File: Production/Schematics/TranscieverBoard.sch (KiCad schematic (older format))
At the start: 6 parts, among them J1 1909763-1, J2 Conn_01x10_Male, J3 Conn_01x10_Male, J4 Conn_01x10_Male, J5 Conn_01x10_Male, U1 MAX7037EGL+

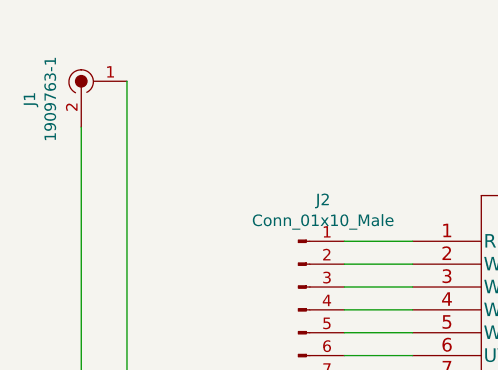
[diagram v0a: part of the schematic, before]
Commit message: Updated PCB
Updated PCB from MCX to SMA
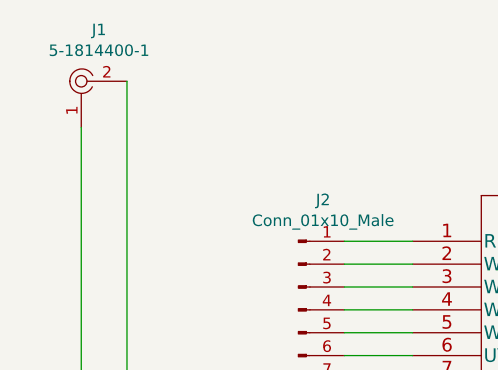
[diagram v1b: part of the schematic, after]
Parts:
- removed J1: 1909763-1, digikey-footprints:UMCoax_Pin_1909763-1, symbol dk_Coaxial-Connectors-RF:1909763-1
- added J1: 5-1814400-1, digikey-footprints:RF_SMA_RightAngle_5-1814400-1, symbol dk_Coaxial-Connectors-RF:5-1814400-1
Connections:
- net at J3.5 (Pin_5), U1.15 (RF_N): now also J1.2
- net at J3.6 (Pin_6), U1.16 (RF_P): now also J1.1
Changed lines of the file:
@@
 	2850 4150 2850 2150
-$Comp
-L dk_Coaxial-Connectors-RF:1909763-1 J1
-U 1 1 61EF2637
-P 2850 1950
-F 0 "J1" H 2928 2175 50  0000 C CNN
-F 1 "1909763-1" H 2928 2084 50  0000 C CNN
-F 2 "digikey-footprints:UMCoax_Pin_1909763-1" H 3050 2150 60  0001 L CNN
-F 3 "https://www.te.com/commerce/DocumentDelivery/DDEController?Action=srchrtrv&DocNm=1909763&DocType=Customer+Drawing&DocLang=English" H 3050 2250 60  0001 L CNN
-F 4 "A118077CT-ND" H 3050 2350 60  0001 L CNN "Digi-Key_PN"
-F 5 "1909763-1" H 3050 2450 60  0001 L CNN "MPN"
-F 6 "Connectors, Interconnects" H 3050 2550 60  0001 L CNN "Category"
-F 7 "Coaxial Connectors (RF)" H 3050 2650 60  0001 L CNN "Family"
-F 8 "https://www.te.com/commerce/DocumentDelivery/DDEController?Action=srchrtrv&DocNm=1909763&DocType=Customer+Drawing&DocLang=English" H 3050 2750 60  0001 L CNN "DK_Datasheet_Link"
-F 9 "/product-detail/en/te-connectivity-amp-connectors/1909763-1/A118077CT-ND/4729711" H 3050 2850 60  0001 L CNN "DK_Detail_Page"
-F 10 "CONN UMCC JACK STR 50OHM SMD" H 3050 2950 60  0001 L CNN "Description"
-F 11 "TE Connectivity AMP Connectors" H 3050 3050 60  0001 L CNN "Manufacturer"
-F 12 "Active" H 3050 3150 60  0001 L CNN "Status"
-	1    2850 1950
-	0    -1   1    0
-$EndComp
 $Comp
 L Connector:Conn_01x10_Male J3
@@
 Wire Wire Line
 	3050 4050 4000 4050
+$Comp
+L dk_Coaxial-Connectors-RF:5-1814400-1 J1
+U 1 1 620A4B48
+P 2850 1950
+F 0 "J1" H 2928 2175 50  0000 C CNN
+F 1 "5-1814400-1" H 2928 2084 50  0000 C CNN
+F 2 "digikey-footprints:RF_SMA_RightAngle_5-1814400-1" H 3050 2150 60  0001 L CNN
+F 3 "https://www.te.com/commerce/DocumentDelivery/DDEController?Action=srchrtrv&DocNm=1814400&DocType=Customer+Drawing&DocLang=English" H 3050 2250 60  0001 L CNN
+F 4 "A97593-ND" H 3050 2350 60  0001 L CNN "Digi-Key_PN"
+F 5 "5-1814400-1" H 3050 2450 60  0001 L CNN "MPN"
+F 6 "Connectors, Interconnects" H 3050 2550 60  0001 L CNN "Category"
+F 7 "Coaxial Connectors (RF)" H 3050 2650 60  0001 L CNN "Family"
+F 8 "https://www.te.com/commerce/DocumentDelivery/DDEController?Action=srchrtrv&DocNm=1814400&DocType=Customer+Drawing&DocLang=English" H 3050 2750 60  0001 L CNN "DK_Datasheet_Link"
+F 9 "/product-detail/en/te-connectivity-amp-connectors/5-1814400-1/A97593-ND/1755981" H 3050 2850 60  0001 L CNN "DK_Detail_Page"
+F 10 "CONN SMA JACK R/A 50 OHM PCB" H 3050 2950 60  0001 L CNN "Description"
+F 11 "TE Connectivity AMP Connectors" H 3050 3050 60  0001 L CNN "Manufacturer"
+F 12 "Active" H 3050 3150 60  0001 L CNN "Status"
+	1    2850 1950
+	1    0    0    -1
+$EndComp
 $EndSCHEMATC

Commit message: PCB Design update
PCB schematic update
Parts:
- removed J1: 5-1814400-1, digikey-footprints:RF_SMA_RightAngle_5-1814400-1, symbol dk_Coaxial-Connectors-RF:5-1814400-1
- removed J3: Conn_01x10_Male, Connector_PinHeader_2.54mm:PinHeader_1x10_P2.54mm_Vertical, symbol Connector:Conn_01x10_Male
- added C10, C12, C6: .1uF, Capacitor_SMD:C_0603_1608Metric, symbol Device:C
- added C22, C23, C24, C29, C32, C36, C5: 220pF, Capacitor_SMD:C_0402_1005Metric, symbol Device:C
- added C26: 820pF, Capacitor_SMD:C_0603_1608Metric, symbol Device:C
- added C3: 1.5pF, Capacitor_SMD:C_0402_1005Metric, symbol Device:C
- added C34, C35: 1.8pF, Capacitor_SMD:C_0402_1005Metric, symbol Device:C
- added J1: 5-1814832-1, digikey-footprints:RF_SMA_Vertical_5-1814832-1, symbol dk_Coaxial-Connectors-RF:5-1814832-1
- added J3: Conn_01x02, Connector_PinHeader_2.54mm:PinHeader_1x02_P2.54mm_Vertical, symbol Connector_Generic:Conn_01x02
- added L4: 100nH, Inductor_SMD:L_0402_1005Metric, symbol Device:L
- added L5, L6, L7, L8, L9: 18nH, Inductor_SMD:L_0402_1005Metric, symbol Device:L
- added R22, R23, R31, R32: 0, Resistor_SMD:R_0402_1005Metric, symbol Device:R
- added U2: C3E-16.000-8-2050-X1-CT, ul_C3E-16-000-8-2050-X1-CT:C3E-16.000-8-2050-X1-CT, symbol ul_C3E-16-000-8-2050-X1-CT:C3E-16.000-8-2050-X1-CT
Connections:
- net GND: now also U1.14 (RFGND1), U1.17 (RFGND2), C10.2, C12.2, C22.2, C23.2, C24.2, C29.1, C32.1, C34.2, C36.2, C5.1, C6.1, U2.2, U2.4
- net at J2.10 (Pin_10), U1.10 (XTIN): now also U2.1
- net at U1.11 (SVDD): now also C5.2, C6.2
- net TEST2: now reaches U1.13 (TEST2)
- net at U1.15 (RF_N): now also C3.1, L6.2, L9.1
- net at U1.16 (RF_P): now also C3.2, L7.1, L9.2
- net at U1.18 (RVDD): now also C10.1, C22.1, J3.2 (Pin_2)
- net at U1.19 (VBG): now also C12.1, C23.1
- net TEST1: now reaches U1.20 (TEST0)
- net at J2.9 (Pin_9), U1.9 (XTOT): now also U2.3
- new net: C26.2, J1.2
- new net: L6.1, R31.2
- new net: L7.2, R32.1
- new net: C34.1, L5.2, R31.1
- new net: C35.1, L8.1, R32.2
- new net: L5.1, R23.1
- new net: C26.1, R22.1, R23.2
- new net: C35.2, R22.2
- new net: C29.2, C32.2, C36.1, L4.2, L8.2
- new net: C24.1, J3.1 (Pin_1), L4.1
